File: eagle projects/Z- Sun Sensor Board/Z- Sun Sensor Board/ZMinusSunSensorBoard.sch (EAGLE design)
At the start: 49 parts, among them U2 ADS7841E_2K5, U4 LM20BIM7X_NOPB, U6 TLV9051IDCKR, U8 TLV9051IDCKR, U9 TLV9051IDCKR

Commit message: Added X & Y sun sensor connectors to Z- Sun Sense Board
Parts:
- removed J6: (no value), my_library:TRM_BLK_1X2
- added C1, C45, C47, C50, C66, C72, C74, C77, C80, C89, C91, C94: 1u, resistor:C-EUC0402
- added C100, C101, C105, C110, C111, C115, C116, C54, C70, C71, C84, C98: 0.022u, resistor:C-EUC0402
- added C102, C104, C107, C109, C112, C114, C46, C48, C49, C51, C53, C65, C67, C69, C73, C75, C76, C78, C79, C81, C83, C86, C88, C90, C92, C93, C95, C97: 0.1u, resistor:C-EUC0402
- added C103, C106, C108, C113, C52, C55, C68, C82, C85, C87, C96, C99: 4.7u, resistor:C-EUC0402
- added J2, J3: HIROSE_FH19C-6S-0.5SH(10), my_library:HIROSE_FH19C-6S-0.5SH(10)
- added JP1: (no value), pinhead:PINHD-1X2
- added R10, R4, R5, R6: 10k, rcl:R-US_R0402
- added R22, R25, R32, R38, R44, R50, R53, R56, R59, R62, R65, R68: 280R, resistor:R-US_R0402
- added R23, R28, R33, R39, R45, R51, R54, R57, R60, R63, R66, R69: 13.7k, resistor:R-US_R0402
- added R24, R31, R34, R40, R46, R52, R55, R58, R61, R64, R67, R70: 3.74k, resistor:R-US_R0402
- added TP10, TP11, TP12, TP13, TP14, TP15, TP16, TP17, TP18, TP19, TP20, TP21, TP22, TP5, TP7, TP9: TESTPOINT, my_library:TESTPOINT
- added U1, U13, U25, U27: ADS7841E_2K5, my_library:ADS7841E_2K5
- added U15, U19, U21, U23, U24, U26, U28, U29, U3, U30, U31, U32: TLV9051IDCKR, my_library:TLV9051IDCKR
- A1: value SUN_SENSOR_MOUNT -> XY_SUN_SENSOR; device my_library:SUN_SENSOR_MOUNT -> my_library:XY_SUN_SENSOR
- J4, J5: value (none) -> HIROSE_FH19C-6S-0.5SH(10); device my_library:TRM_BLK_1X2 -> my_library:HIROSE_FH19C-6S-0.5SH(10)
- JP3: device pinhead:PINHD-1X6 -> pinhead:PINHD-2X5
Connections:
- new net !CS!_SUN_X+: JP3.2, U25.!CS
- new net !CS!_SUN_X-: JP3.7, U13.!CS
- new net !CS!_SUN_Y+: JP3.4, U27.!CS
- new net !CS!_SUN_Y-: JP3.9, U1.!CS
- new net !CS!_SUN_Z-: JP3.6
- new net N$10: TP13.TP, U13.CH0
- new net N$11: TP21.TP, U27.CH0
- new net N$14: TP22.TP, U1.CH0
- new net N$22: C51.1, R5.1, U13.!SHDN
- new net N$23: C100.1, J5.3, R31.1, U23.-
- new net N$24: C81.1, R10.1, U1.!SHDN
- new net N$25: C95.1, R6.1, U27.!SHDN
- new net N$29: C84.1, J5.1, R24.1, U3.-
- new net N$31: R22.2, R23.1, U3.+
- new net N$34: R25.2, R28.1, U23.+
- new net N$35: C101.1, J5.5, R34.1, U24.-
- new net N$36: R32.2, R33.1, U24.+
- new net N$37: C98.1, J4.1, R64.1, U30.-
- new net N$38: C54.1, J3.1, R40.1, U15.-
- new net N$4: C102.1, R4.1, U25.!SHDN
- new net N$41: R38.2, R39.1, U15.+
- new net N$44: C70.1, J3.3, R46.1, U19.-
- new net N$45: R44.2, R45.1, U19.+
- new net N$46: C71.1, J3.5, R52.1, U21.-
- new net N$47: R50.2, R51.1, U21.+
- new net N$49: C105.1, J2.1, R55.1, U26.-
- new net N$5: TP17.TP, U25.CH0
- new net N$54: R53.2, R54.1, U26.+
- new net N$55: C110.1, J2.3, R58.1, U28.-
- new net N$56: R56.2, R57.1, U28.+
- new net N$57: C111.1, J2.5, R61.1, U29.-
- new net N$58: R59.2, R60.1, U29.+
- new net N$61: R62.2, R63.1, U30.+
- new net N$63: C115.1, J4.3, R67.1, U31.-
- new net N$64: R65.2, R66.1, U31.+
- new net N$65: C116.1, J4.5, R70.1, U32.-
- new net N$66: R68.2, R69.1, U32.+
- new net N$67: JP3.8
- new net N$68: JP3.10
- new net X+_0_DEGREES: C105.2, R55.2, TP14.TP, U25.CH1, U26.OUT
- new net X+_120_DEGREES: C110.2, R58.2, TP15.TP, U25.CH2, U28.OUT
- new net X+_240_DEGREES: C111.2, R61.2, TP16.TP, U25.CH3, U29.OUT
- new net X-_0_DEGREES: C54.2, R40.2, TP10.TP, U13.CH1, U15.OUT
- new net X-_120_DEGREES: C70.2, R46.2, TP11.TP, U13.CH2, U19.OUT
- new net X-_240_DEGREES: C71.2, R52.2, TP12.TP, U13.CH3, U21.OUT
- new net Y+_0_DEGREES: C98.2, R64.2, TP18.TP, U27.CH1, U30.OUT
- new net Y+_120_DEGREES: C115.2, R67.2, TP19.TP, U27.CH2, U31.OUT
- new net Y+_240_DEGREES: C116.2, R70.2, TP20.TP, U27.CH3, U32.OUT
- new net Y-_0_DEGREES: C84.2, R24.2, TP5.TP, U1.CH1, U3.OUT
- new net Y-_120_DEGREES: C100.2, R31.2, TP7.TP, U1.CH2, U23.OUT
- new net Y-_240_DEGREES: C101.2, R34.2, TP9.TP, U1.CH3, U24.OUT
- net !CS!_SUN_Z+: no longer JP3.3
- net +3V3: now also C1.1, C103.1, C104.1, C106.1, C107.1, C108.1, C109.1, C112.1, C113.1, C114.1, C45.1, C46.1, C47.1, C48.1, C49.1, C50.1, C52.1, C53.1, C55.1, C65.1, C66.1, C67.1, C68.1, C69.1, C72.1, C73.1, C74.1, C75.1, C76.1, C77.1, C78.1, C79.1, C80.1, C82.1, C83.1, C85.1, C86.1, C87.1, C88.1, C89.1, C90.1, C91.1, C92.1, C93.1, C94.1, C96.1, C97.1, C99.1, JP1.1, R10.2, R23.2, R28.2, R33.2, R39.2, R4.2, R45.2, R5.2, R51.2, R54.2, R57.2, R6.2, R60.2, R63.2, R66.2, R69.2, U1.VCC+, U1.VCC+_2, U1.VREF, U13.VCC+, U13.VCC+_2, U13.VREF, U15.V+, U19.V+, U21.V+, U23.V+, U24.V+, U25.VCC+, U25.VCC+_2, U25.VREF, U26.V+, U27.VCC+, U27.VCC+_2, U27.VREF, U28.V+, U29.V+, U3.V+, U30.V+, U31.V+, U32.V+; no longer JP3.6
- net 0_DEGREES: now also U2.CH2; no longer U2.CH1
- net 120_DEGREES: now also U2.CH3; no longer U2.CH2
- net 240_DEGREES: now also U2.CH1; no longer U2.CH3
- net GND: now also A1G$2.A1, A1G$2.A2, A1G$2.A3, C1.2, C102.2, C103.2, C104.2, C106.2, C107.2, C108.2, C109.2, C112.2, C113.2, C114.2, C45.2, C46.2, C47.2, C48.2, C49.2, C50.2, C51.2, C52.2, C53.2, C55.2, C65.2, C66.2, C67.2, C68.2, C69.2, C72.2, C73.2, C74.2, C75.2, C76.2, C77.2, C78.2, C79.2, C80.2, C81.2, C82.2, C83.2, C85.2, C86.2, C87.2, C88.2, C89.2, C90.2, C91.2, C92.2, C93.2, C94.2, C95.2, C96.2, C97.2, C99.2, J2.2, J2.4, J2.6, J2.MTGTAB1, J2.MTGTAB2, J3.2, J3.4, J3.6, J3.MTGTAB1, J3.MTGTAB2, J4.2, J4.4, J4.6, J4.MTGTAB1, J4.MTGTAB2, J5.2, J5.4, J5.6, J5.MTGTAB1, J5.MTGTAB2, JP1.2, R22.1, R25.1, R32.1, R38.1, R44.1, R50.1, R53.1, R56.1, R59.1, R62.1, R65.1, R68.1, U1.COM, U1.GND, U1.MODE, U13.COM, U13.GND, U13.MODE, U15.V-, U19.V-, U21.V-, U23.V-, U24.V-, U25.COM, U25.GND, U25.MODE, U26.V-, U27.COM, U27.GND, U27.MODE, U28.V-, U29.V-, U3.V-, U30.V-, U31.V-, U32.V-; no longer J4.1, J5.1, J6.1, JP3.1
- net N$12: now also A1G$2.C3; no longer J4.2
- net N$3: now also A1G$2.C1; no longer J6.2
- net N$8: now also A1G$2.C2; no longer J5.2
- net UCB0_SPI_CLK: now also JP3.5, U1.DCLK, U13.DCLK, U25.DCLK, U27.DCLK; no longer JP3.2
- net UCB0_SPI_MISO: now also JP3.1, U1.DOUT, U13.DOUT, U25.DOUT, U27.DOUT; no longer JP3.5
- net UCB0_SPI_MOSI: now also JP3.3, U1.DIN, U13.DIN, U25.DIN, U27.DIN; no longer JP3.4
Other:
- note added: "A"
- note added: "Custom machine sun sensor mount for Z- face photodiodes mechanically to board"
- note added: "NC"

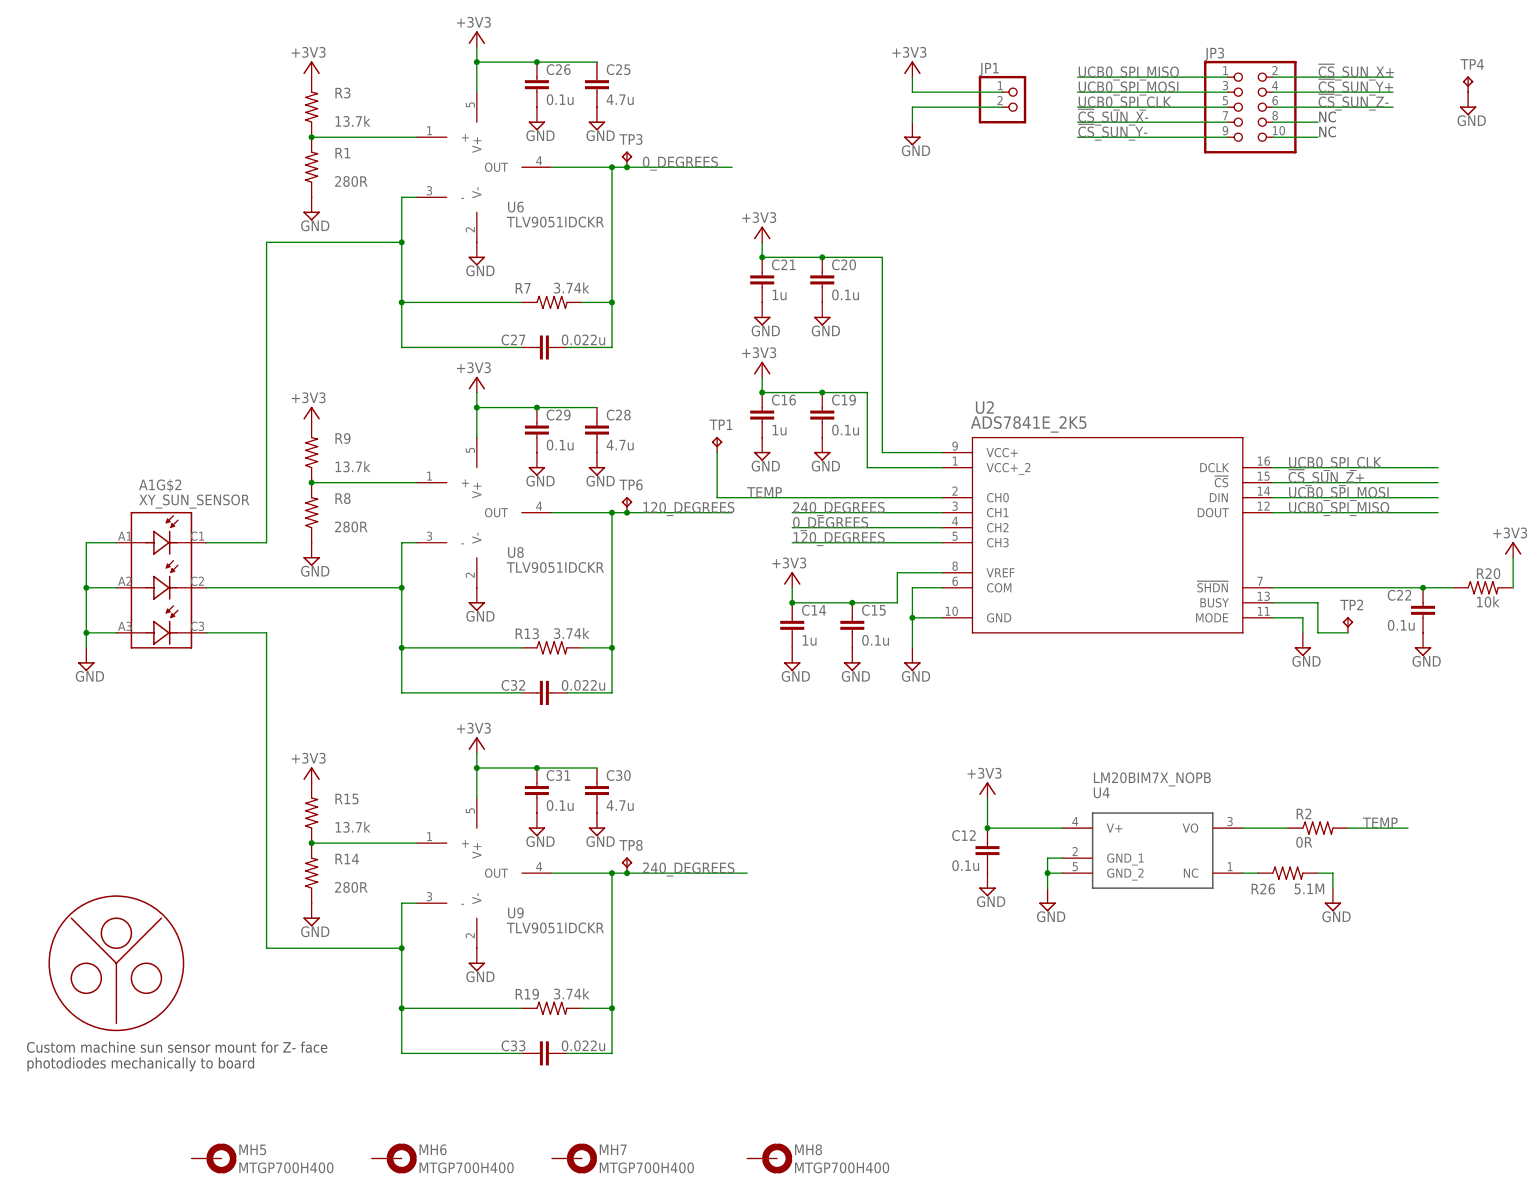
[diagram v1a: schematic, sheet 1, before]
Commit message: Added indicator LED
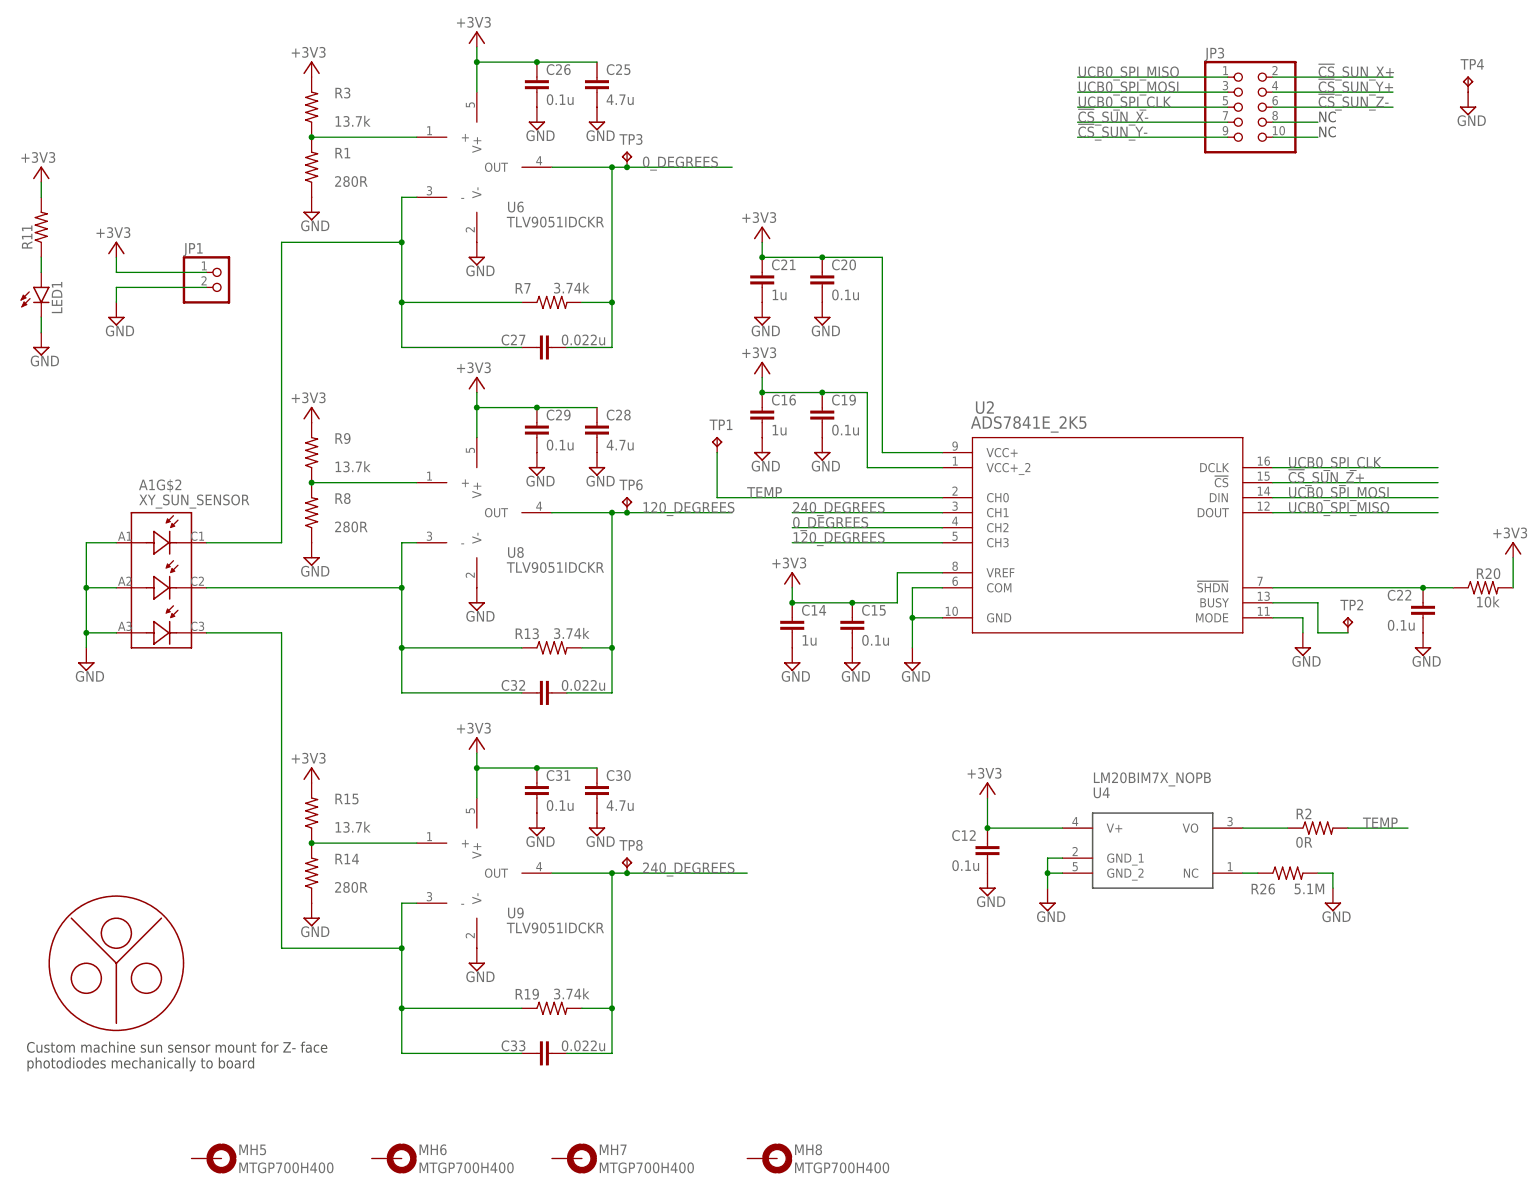
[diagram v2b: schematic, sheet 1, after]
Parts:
- added LED1: (no value), led:LEDCHIP-LED0603
- added R11: (no value), rcl:R-US_R0603
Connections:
- new net N$48: LED1.A, R11.1
- net +3V3: now also R11.2
- net GND: now also LED1.C
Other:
- moved on the sheet: JP1
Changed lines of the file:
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@@
 <part name="SUPPLY14" library="supply2" library_urn="urn:adsk.eagle:library:372" deviceset="GND" device=""/>
 <part name="JP3" library="pinhead" library_urn="urn:adsk.eagle:library:325" deviceset="PINHD-2X5" device="" package3d_urn="urn:adsk.eagle:package:22470/2"/>
+<part name="LED1" library="led" library_urn="urn:adsk.eagle:library:259" deviceset="LED" device="CHIP-LED0603" package3d_urn="urn:adsk.eagle:package:15819/3"/>
+<part name="R11" library="rcl" library_urn="urn:adsk.eagle:library:334" deviceset="R-US_" device="R0603" package3d_urn="urn:adsk.eagle:package:23555/3"/>
+<part name="+3V23" library="supply1" library_urn="urn:adsk.eagle:library:371" deviceset="+3V3" device=""/>
+<part name="SUPPLY1" library="supply2" library_urn="urn:adsk.eagle:library:372" deviceset="GND" device=""/>
 </parts>
 <sheets>
@@
 <attribute name="VALUE" x="18.415" y="90.805" size="1.778" layer="96"/>
 </instance>
-<instance part="+3V22" gate="G$1" x="160.02" y="195.58" smashed="yes" grouprefs="POWER">
-<attribute name="VALUE" x="162.56" y="198.12" size="1.778" layer="96" rot="R180"/>
-</instance>
-<instance part="SUPPLY9" gate="GND" x="160.02" y="182.88" smashed="yes" grouprefs="POWER">
-<attribute name="VALUE" x="158.115" y="179.705" size="1.778" layer="96"/>
-</instance>
-<instance part="JP1" gate="G$1" x="177.8" y="187.96" smashed="yes" grouprefs="POWER">
-<attribute name="NAME" x="171.45" y="193.675" size="1.778" layer="95"/>
-<attribute name="VALUE" x="171.45" y="182.88" size="1.778" layer="96"/>
+<instance part="+3V22" gate="G$1" x="25.4" y="165.1" smashed="yes" grouprefs="POWER">
+<attribute name="VALUE" x="27.94" y="167.64" size="1.778" layer="96" rot="R180"/>
+</instance>
+<instance part="SUPPLY9" gate="GND" x="25.4" y="152.4" smashed="yes" grouprefs="POWER">
+<attribute name="VALUE" x="23.495" y="149.225" size="1.778" layer="96"/>
+</instance>
+<instance part="JP1" gate="G$1" x="43.18" y="157.48" smashed="yes" grouprefs="POWER">
+<attribute name="NAME" x="36.83" y="163.195" size="1.778" layer="95"/>
+<attribute name="VALUE" x="36.83" y="152.4" size="1.778" layer="96"/>
 </instance>
 <instance part="JP3" gate="A" x="215.9" y="187.96" smashed="yes">
 <attribute name="NAME" x="209.55" y="196.215" size="1.778" layer="95"/>
 <attribute name="VALUE" x="209.55" y="177.8" size="1.778" layer="96"/>
+</instance>
+<instance part="LED1" gate="G$1" x="12.7" y="157.48" smashed="yes" grouprefs="POWER">
+<attribute name="NAME" x="16.256" y="152.908" size="1.778" layer="95" rot="R90"/>
+<attribute name="VALUE" x="18.415" y="152.908" size="1.778" layer="96" rot="R90"/>
+</instance>
+<instance part="R11" gate="G$1" x="12.7" y="167.64" smashed="yes" rot="R90" grouprefs="POWER">
+<attribute name="NAME" x="11.2014" y="163.83" size="1.778" layer="95" rot="R90"/>
+<attribute name="VALUE" x="16.002" y="163.83" size="1.778" layer="96" rot="R90"/>
+</instance>
+<instance part="+3V23" gate="G$1" x="12.7" y="177.8" smashed="yes" grouprefs="POWER">
+<attribute name="VALUE" x="15.24" y="180.34" size="1.778" layer="96" rot="R180"/>
+</instance>
+<instance part="SUPPLY1" gate="GND" x="12.7" y="147.32" smashed="yes" grouprefs="POWER">
+<attribute name="VALUE" x="10.795" y="144.145" size="1.778" layer="96"/>
 </instance>
 </instances>
@@
 </segment>
 <segment>
-<wire x1="160.02" y1="193.04" x2="160.02" y2="190.5" width="0.1524" layer="91" grouprefs="POWER"/>
-<wire x1="160.02" y1="190.5" x2="175.26" y2="190.5" width="0.1524" layer="91" grouprefs="POWER"/>
+<wire x1="25.4" y1="162.56" x2="25.4" y2="160.02" width="0.1524" layer="91" grouprefs="POWER"/>
+<wire x1="25.4" y1="160.02" x2="40.64" y2="160.02" width="0.1524" layer="91" grouprefs="POWER"/>
 <pinref part="+3V22" gate="G$1" pin="+3V3"/>
 <pinref part="JP1" gate="G$1" pin="1"/>
+</segment>
+<segment>
+<pinref part="R11" gate="G$1" pin="2"/>
+<pinref part="+3V23" gate="G$1" pin="+3V3"/>
+<wire x1="12.7" y1="172.72" x2="12.7" y2="175.26" width="0.1524" layer="91" grouprefs="POWER"/>
 </segment>
 </net>
@@
 <pinref part="SUPPLY9" gate="GND" pin="GND"/>
 <pinref part="JP1" gate="G$1" pin="2"/>
-<wire x1="175.26" y1="187.96" x2="160.02" y2="187.96" width="0.1524" layer="91" grouprefs="POWER"/>
-<wire x1="160.02" y1="187.96" x2="160.02" y2="185.42" width="0.1524" layer="91" grouprefs="POWER"/>
+<wire x1="40.64" y1="157.48" x2="25.4" y2="157.48" width="0.1524" layer="91" grouprefs="POWER"/>
+<wire x1="25.4" y1="157.48" x2="25.4" y2="154.94" width="0.1524" layer="91" grouprefs="POWER"/>
+</segment>
+<segment>
+<pinref part="SUPPLY1" gate="GND" pin="GND"/>
+<pinref part="LED1" gate="G$1" pin="C"/>
+<wire x1="12.7" y1="149.86" x2="12.7" y2="152.4" width="0.1524" layer="91" grouprefs="POWER"/>
 </segment>
 </net>
@@
 <pinref part="C27" gate="G$1" pin="1"/>
 <pinref part="R7" gate="G$1" pin="1"/>
-<wire x1="73.66" y1="165.1" x2="50.8" y2="165.1" width="0.1524" layer="91"/>
+<wire x1="73.66" y1="165.1" x2="53.34" y2="165.1" width="0.1524" layer="91"/>
 <junction x="73.66" y="165.1"/>
 <pinref part="A1" gate="G$2" pin="C1"/>
-<wire x1="40.64" y1="114.3" x2="50.8" y2="114.3" width="0.1524" layer="91"/>
-<wire x1="50.8" y1="114.3" x2="50.8" y2="165.1" width="0.1524" layer="91"/>
+<wire x1="40.64" y1="114.3" x2="53.34" y2="114.3" width="0.1524" layer="91"/>
+<wire x1="53.34" y1="114.3" x2="53.34" y2="165.1" width="0.1524" layer="91"/>
 </segment>
 </net>
@@
 <wire x1="73.66" y1="53.34" x2="76.2" y2="53.34" width="0.1524" layer="91"/>
 <pinref part="R19" gate="G$1" pin="1"/>
-<wire x1="73.66" y1="45.72" x2="50.8" y2="45.72" width="0.1524" layer="91"/>
+<wire x1="73.66" y1="45.72" x2="53.34" y2="45.72" width="0.1524" layer="91"/>
 <junction x="73.66" y="45.72"/>
 <pinref part="C33" gate="G$1" pin="1"/>
 <pinref part="A1" gate="G$2" pin="C3"/>
-<wire x1="40.64" y1="99.06" x2="50.8" y2="99.06" width="0.1524" layer="91"/>
-<wire x1="50.8" y1="99.06" x2="50.8" y2="45.72" width="0.1524" layer="91"/>
+<wire x1="40.64" y1="99.06" x2="53.34" y2="99.06" width="0.1524" layer="91"/>
+<wire x1="53.34" y1="99.06" x2="53.34" y2="45.72" width="0.1524" layer="91"/>
 </segment>
 </net>
@@
 </segment>
 </net>
+<net name="N$48" class="0">
+<segment>
+<pinref part="LED1" gate="G$1" pin="A"/>
+<pinref part="R11" gate="G$1" pin="1"/>
+<wire x1="12.7" y1="160.02" x2="12.7" y2="162.56" width="0.1524" layer="91" grouprefs="POWER"/>
+</segment>
+</net>
